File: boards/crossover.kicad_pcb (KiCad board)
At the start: 2 copper layers, 160 x 105.4 mm, 61 parts, among them J1 JACK_TRS_6PINS, P1 12-0-12, U1 TL072, U2 TL074, U3 TDA7292, U4 TL074

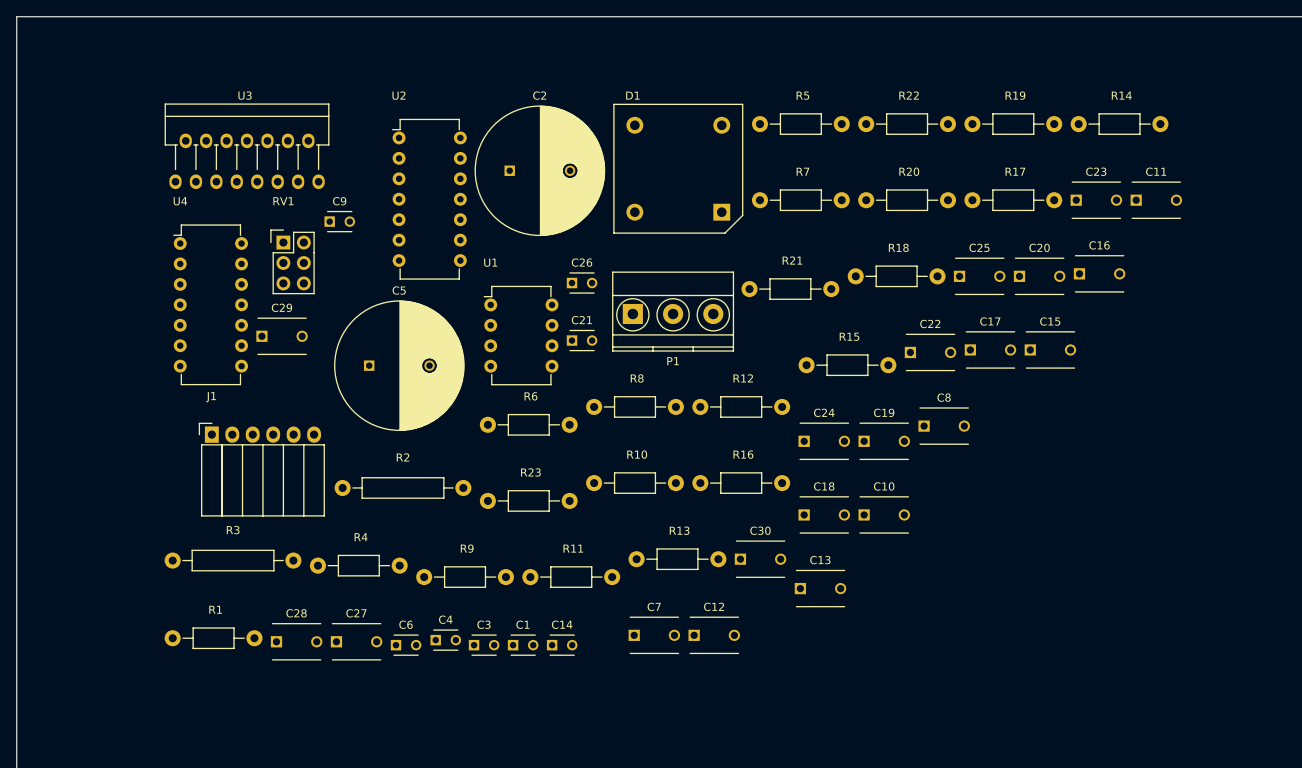
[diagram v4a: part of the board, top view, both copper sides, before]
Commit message: first working impedance measurements
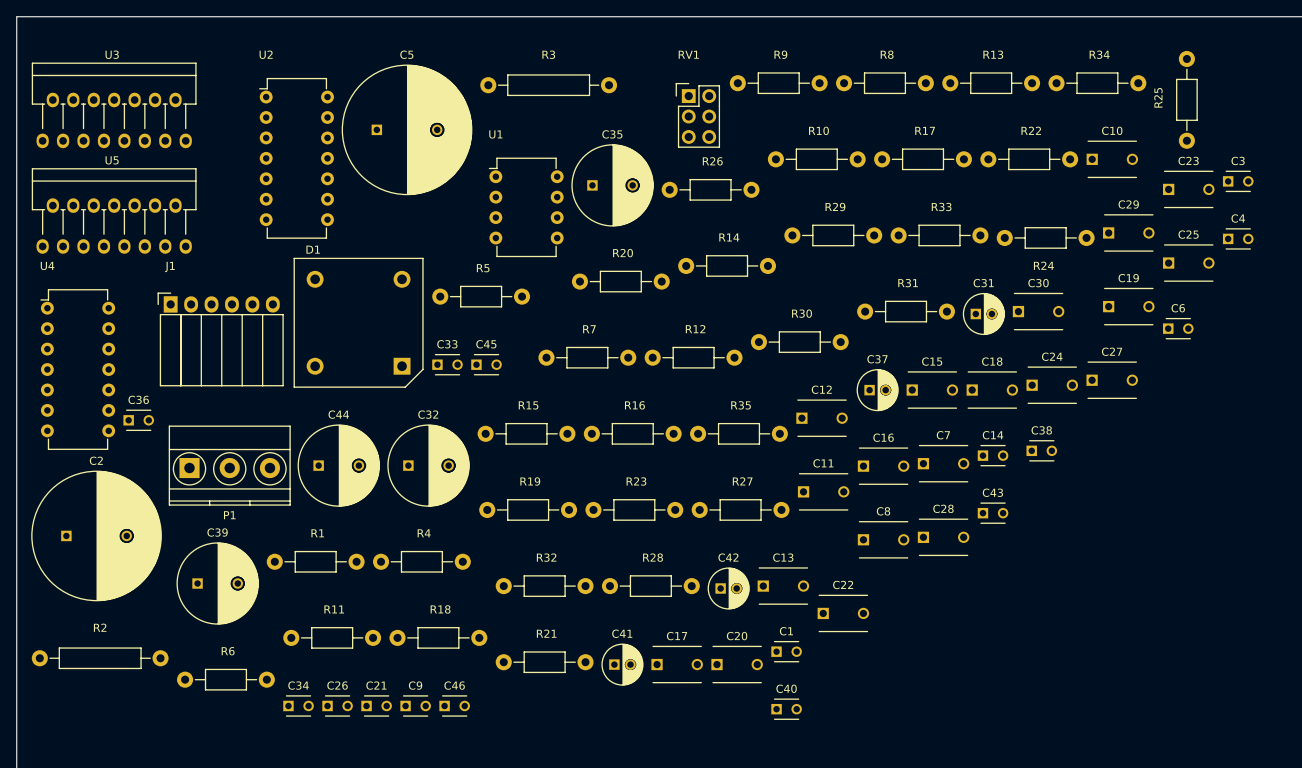
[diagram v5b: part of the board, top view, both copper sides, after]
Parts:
- added C31: CP, Capacitors_ThroughHole:C_Radial_D5_L11_P2, F.Cu at (210.6, 90.3)
- added C32: 1000u, Capacitors_ThroughHole:C_Radial_D10_L20_P5, F.Cu at (140.1, 109.1)
- added C33: 100n, Capacitors_ThroughHole:C_Disc_D3_P2.5, F.Cu at (143.7, 96.6)
- added C34: 100n, Capacitors_ThroughHole:C_Disc_D3_P2.5, F.Cu at (125.2, 139.0)
- added C35: 1000u, Capacitors_ThroughHole:C_Radial_D10_L20_P5, F.Cu at (163.0, 74.3)
- added C36: 100n, Capacitors_ThroughHole:C_Disc_D3_P2.5, F.Cu at (105.4, 103.5)
- added C37: CP, Capacitors_ThroughHole:C_Radial_D5_L11_P2, F.Cu at (197.4, 99.7)
- added C38: 100n, Capacitors_ThroughHole:C_Disc_D3_P2.5, F.Cu at (217.6, 107.3)
- added C39: 1000u, Capacitors_ThroughHole:C_Radial_D10_L20_P5, F.Cu at (113.9, 123.8)
- added C40: 100n, Capacitors_ThroughHole:C_Disc_D3_P2.5, F.Cu at (185.9, 139.4)
- added C41: CP, Capacitors_ThroughHole:C_Radial_D5_L11_P2, F.Cu at (165.7, 133.9)
- added C42: CP, Capacitors_ThroughHole:C_Radial_D5_L11_P2, F.Cu at (178.9, 124.4)
- added C43: 100n, Capacitors_ThroughHole:C_Disc_D3_P2.5, F.Cu at (211.5, 115.0)
- added C44: 1000u, Capacitors_ThroughHole:C_Radial_D10_L20_P5, F.Cu at (129.0, 109.1)
- added C45: 100n, Capacitors_ThroughHole:C_Disc_D3_P2.5, F.Cu at (148.6, 96.6)
- added C46: 100n, Capacitors_ThroughHole:C_Disc_D3_P2.5, F.Cu at (144.6, 139.0)
- added R24: 18K, Resistors_ThroughHole:Resistor_Horizontal_RM10mm, F.Cu at (224.4, 80.8)
- added R25: 560R, Resistors_ThroughHole:Resistor_Horizontal_RM10mm, F.Cu at (236.9, 68.8)
- added R26: 4.8R, Resistors_ThroughHole:Resistor_Horizontal_RM10mm, F.Cu at (172.6, 74.9)
- added R27: 18K, Resistors_ThroughHole:Resistor_Horizontal_RM10mm, F.Cu at (176.3, 114.6)
- added R28: 4.8R, Resistors_ThroughHole:Resistor_Horizontal_RM10mm, F.Cu at (165.2, 124.1)
- added R29: 560R, Resistors_ThroughHole:Resistor_Horizontal_RM10mm, F.Cu at (187.8, 80.5)
- added R30: 18K, Resistors_ThroughHole:Resistor_Horizontal_RM10mm, F.Cu at (183.7, 93.8)
- added R31: 4.8R, Resistors_ThroughHole:Resistor_Horizontal_RM10mm, F.Cu at (196.9, 90.0)
- added R32: 560R, Resistors_ThroughHole:Resistor_Horizontal_RM10mm, F.Cu at (152.0, 124.1)
- added R33: 18K, Resistors_ThroughHole:Resistor_Horizontal_RM10mm, F.Cu at (201.0, 80.5)
- added R34: 4.8R, Resistors_ThroughHole:Resistor_Horizontal_RM10mm, F.Cu at (220.7, 61.6)
- added R35: 560R, Resistors_ThroughHole:Resistor_Horizontal_RM10mm, F.Cu at (176.1, 105.2)
- added U5: TDA7292, TO_SOT_Packages_THT:Multiwatt_15_Vertical, F.Cu at (94.7, 81.9)
- moved C4 110.4 mm to (242.0, 81.0)
- moved C3 110.0 mm to (242.0, 73.8)
- moved C29 106.0 mm to (227.1, 80.2)
- moved C6 103.7 mm to (234.5, 92.1)
- moved C27 99.4 mm to (225.1, 98.5)
- moved C28 81.4 mm to (204.1, 118.0)
- moved R19 77.0 mm to (149.9, 114.6)
- moved R9 72.7 mm to (181.1, 61.6)
- moved R18 72.5 mm to (138.8, 130.5)
- moved C2 71.4 mm to (97.6, 117.9)
- moved R3 70.9 mm to (150.0, 61.9)
- moved R13 70.8 mm to (207.5, 61.6)
- moved C20 61.2 mm to (178.5, 133.8)
- moved C9 60.9 mm to (139.8, 139.0)
- moved C26 60.7 mm to (130.1, 139.0)
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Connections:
- net left_high_out renamed Net-(C42-Pad2)
- net left_low_out renamed Net-(C22-Pad1)
- C10 pad 1: right_low_out -> Net-(C10-Pad1)
- C11 pad 1: right_low_out -> Net-(C10-Pad1)
- R9 pad 2: right_high_out -> Net-(C37-Pad2)
- U2 pad 13: right_high_out -> Net-(C37-Pad2)
- U2 pad 14: right_high_out -> Net-(C37-Pad2)
- U2 pad 6: right_low_out -> Net-(C10-Pad1)
- U2 pad 7: right_low_out -> Net-(C10-Pad1)
- U3 pad 1: (no net) -> -12V
- U3 pad 10: (no net) -> Net-(R27-Pad1)
- U3 pad 11: (no net) -> Net-(C37-Pad1)
- U3 pad 2: (no net) -> right_high_out
- U3 pad 3: (no net) -> +12V
- U3 pad 4: (no net) -> right_low_out
- U3 pad 6: (no net) -> -12V
- U3 pad 7: (no net) -> Net-(C31-Pad1)
- U3 pad 8: (no net) -> Net-(R24-Pad1)
- U3 pad 9: (no net) -> GND

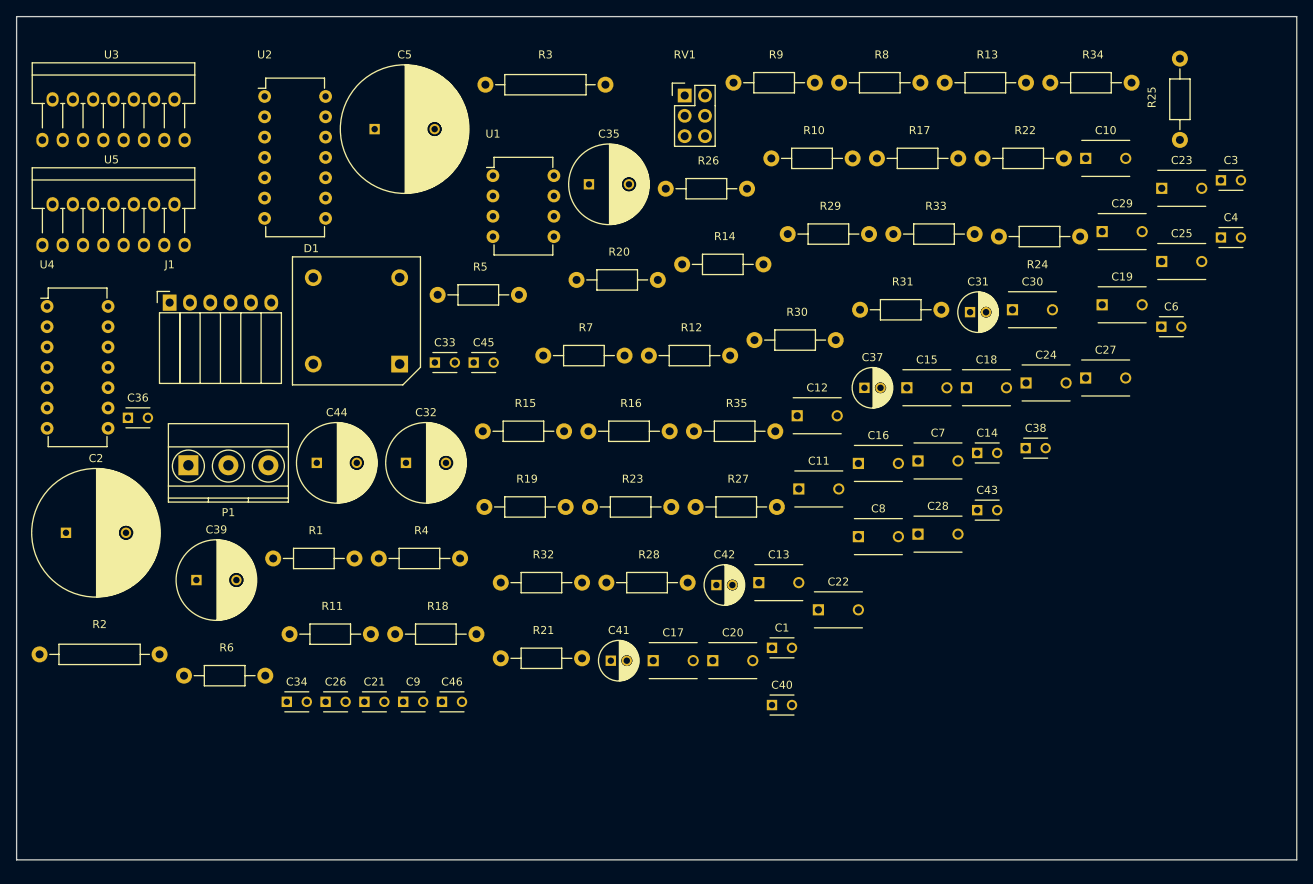
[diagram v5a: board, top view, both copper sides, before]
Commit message: documentation, pcb updates, some pylint fixes
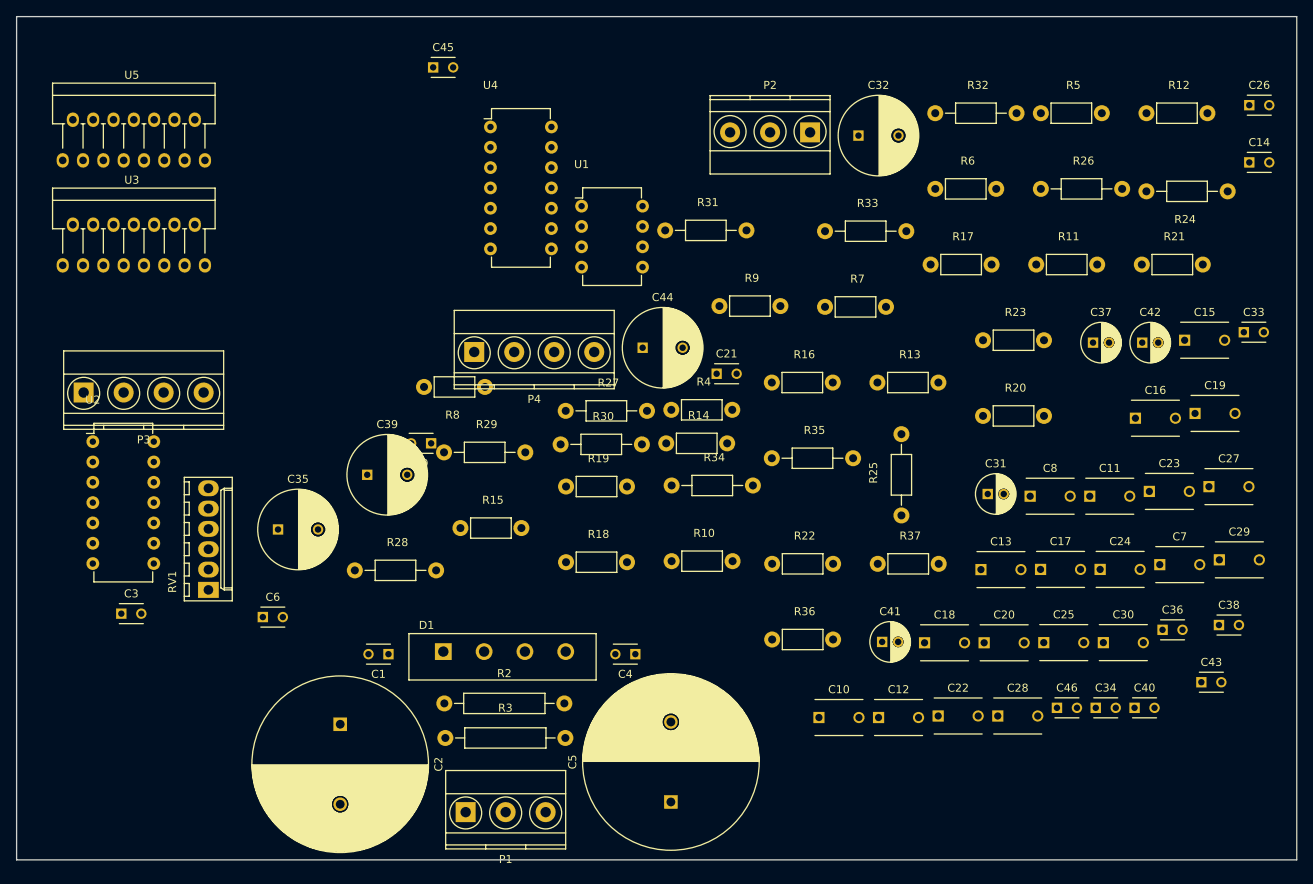
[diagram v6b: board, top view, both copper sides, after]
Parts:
- removed J1: JACK_TRS_6PINS, Socket_Strips:Socket_Strip_Angled_1x06
- removed R1: 100, Resistors_ThroughHole:Resistor_Horizontal_RM10mm
- added P2: CONN_01X03, Terminal_Blocks:TerminalBlock_Pheonix_MKDS1.5-3pol, F.Cu at (190.6, 67.8)
- added P3: CONN_01X04, Terminal_Blocks:TerminalBlock_Pheonix_MKDS1.5-4pol, F.Cu at (99.8, 100.3)
- added P4: CONN_01X04, Terminal_Blocks:TerminalBlock_Pheonix_MKDS1.5-4pol, F.Cu at (148.6, 95.3)
- added R36: 1K, Resistors_ThroughHole:Resistor_Horizontal_RM7mm, F.Cu at (185.9, 131.2)
- added R37: 1K, Resistors_ThroughHole:Resistor_Horizontal_RM7mm, F.Cu at (199.1, 121.7)
- C2, C5: footprint Capacitors_ThroughHole:C_Radial_D16_L31.5_P7.5 -> Capacitors_ThroughHole:C_Radial_D22_L41_P10
- C31, C37, C41, C42: value CP -> 1u
- D1: footprint Diodes_ThroughHole:Diode_Bridge_15.7x15.7 -> Diodes_ThroughHole:Diode_Bridge_18.5x5.5
- P1: value 12-0-12 -> CONN_01X03
- R10, R11, R16, R17, R18, R19, R20, R21, R22, R23, R8, R9: value RH -> R; footprint Resistors_ThroughHole:Resistor_Horizontal_RM10mm -> Resistors_ThroughHole:Resistor_Horizontal_RM7mm
- R12, R13, R14, R15, R4, R5, R6, R7: value RL -> R; footprint Resistors_ThroughHole:Resistor_Horizontal_RM10mm -> Resistors_ThroughHole:Resistor_Horizontal_RM7mm
- RV1: footprint Pin_Headers:Pin_Header_Straight_2x03 -> Connectors_Molex:Molex_KK-6410-06_06x2.54mm_Straight
- moved C3 147.7 mm to (104.5, 128.0)
- moved C26 137.5 mm to (245.5, 64.4)
- moved C36 132.0 mm to (234.7, 130.0)
- moved C6 118.0 mm to (122.2, 128.4)
- moved R6 111.9 mm to (206.3, 74.9)
- moved R11 104.1 mm to (218.9, 84.3)
- moved C33 101.2 mm to (244.8, 92.8)
- moved C34 101.1 mm to (226.3, 139.7)
- moved R21 94.0 mm to (232.1, 84.3)
- moved C5 91.9 mm to (173.2, 151.5), turned to 90 degrees
- moved C4 89.8 mm to (168.8, 133.0), turned to 180 degrees
- moved RV1 85.8 mm to (115.4, 125.0), turned to 90 degrees
- moved R3 81.8 mm to (145.0, 143.5)
- moved R32 80.0 mm to (206.3, 65.4)
- moved R5 78.7 mm to (219.5, 65.4)
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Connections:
- net Net-(D1-Pad2) renamed /-12VAC
- net Net-(D1-Pad4) renamed /+12VAC
- net left_high_out renamed /left_high_out
- net left_low_out renamed /left_low_out
- net right_high_out renamed /right_high_out
- net right_low_out renamed /right_low_out
- C32 pad 2: GND -> Net-(C32-Pad2)
- C39 pad 2: GND -> Net-(C39-Pad2)
- RV1 pad 1: Net-(J1-Pad2) -> right_in
- RV1 pad 4: Net-(J1-Pad3) -> left_in
- U3 pad 5: (no net) -> Net-(C32-Pad2)
- U5 pad 5: (no net) -> Net-(C39-Pad2)

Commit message: some board updates
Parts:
- added C47: 1000u, Capacitors_ThroughHole:C_Radial_D10_L20_P5, F.Cu at (287.0, 84.8)
- added C48: 100n, Capacitors_ThroughHole:C_Disc_D3_P2.5, F.Cu at (149.1, 72.5)
- added C49: 100n, Capacitors_ThroughHole:C_Disc_D6_P5, F.Cu at (143.4, 68.3)
- added C50: 100n, Capacitors_ThroughHole:C_Disc_D3_P2.5, F.Cu at (162.9, 74.0)
- added C51: 100n, Capacitors_ThroughHole:C_Disc_D6_P5, F.Cu at (142.9, 79.6)
- added C52: 100n, Capacitors_ThroughHole:C_Disc_D6_P5, F.Cu at (168.0, 66.7)
- added C53: 100n, Capacitors_ThroughHole:C_Disc_D6_P5, F.Cu at (168.4, 78.4)
- added C54: 100n, Capacitors_ThroughHole:C_Disc_D3_P2.5, F.Cu at (107.4, 88.9)
- added C55: 100n, Capacitors_ThroughHole:C_Disc_D3_P2.5, F.Cu at (109.0, 73.4)
- added R1: 2K2, Resistors_ThroughHole:Resistor_Horizontal_RM7mm, F.Cu at (138.4, 75.9)
- added R38: Rph, Resistors_ThroughHole:Resistor_Horizontal_RM7mm, F.Cu at (140.8, 60.7)
- added R39: 2K2, Resistors_ThroughHole:Resistor_Horizontal_RM7mm, F.Cu at (149.5, 84.5)
- added R40: 2K2, Resistors_ThroughHole:Resistor_Horizontal_RM7mm, F.Cu at (157.2, 88.0)
- added R41: Rph, Resistors_ThroughHole:Resistor_Horizontal_RM7mm, F.Cu at (138.3, 87.2)
- added R42: 2K2, Resistors_ThroughHole:Resistor_Horizontal_RM7mm, F.Cu at (172.0, 59.6)
- added R43: 2K2, Resistors_ThroughHole:Resistor_Horizontal_RM7mm, F.Cu at (160.4, 61.0)
- added R44: 2K2, Resistors_ThroughHole:Resistor_Horizontal_RM7mm, F.Cu at (172.0, 77.9)
- added R45: 2K2, Resistors_ThroughHole:Resistor_Horizontal_RM7mm, F.Cu at (172.1, 88.6)
- added R46: Rph, Resistors_ThroughHole:Resistor_Horizontal_RM7mm, F.Cu at (150.9, 58.2)
- added R47: Rph, Resistors_ThroughHole:Resistor_Horizontal_RM7mm, F.Cu at (168.4, 87.9)
- added R48: Rbs1, Resistors_ThroughHole:Resistor_Horizontal_RM7mm, F.Cu at (107.3, 92.8)
- added R49: Rbs2, Resistors_ThroughHole:Resistor_Horizontal_RM7mm, F.Cu at (110.1, 92.8)
- added R50: Rbs1, Resistors_ThroughHole:Resistor_Horizontal_RM7mm, F.Cu at (120.7, 70.1)
- added R51: Rbs2, Resistors_ThroughHole:Resistor_Horizontal_RM7mm, F.Cu at (113.0, 67.1)
- added RV2: 1K POT, Potentiometers:Potentiometer_Bourns_3339P_Angular_ScrewUp, F.Cu at (253.1, 111.1)
- added RV3: 1K POT, Potentiometers:Potentiometer_Bourns_3339P_Angular_ScrewUp, F.Cu at (264.5, 101.5)
- added U6: TL074, Housings_DIP:DIP-14_W7.62mm, F.Cu at (152.4, 65.8)
- R24, R30: value 18K -> 68K
- R25, R32: value 560R -> 1K5
- R37: value 1K -> 2K2
- moved C9 219.8 mm to (363.0, 103.8)
- moved C45 203.5 mm to (337.0, 122.7)
- moved C12 200.7 mm to (381.8, 57.8)
- moved R22 196.3 mm to (371.4, 57.8)
- moved R15 193.5 mm to (336.2, 76.7)
- moved R4 192.8 mm to (360.8, 57.8)
- moved C21 192.1 mm to (371.0, 93.7)
- moved C39 185.7 mm to (314.1, 60.6)
- moved R8 185.1 mm to (334.9, 91.8)
- moved R30 184.1 mm to (336.9, 57.8)
- moved R28 183.0 mm to (309.8, 72.5)
- moved R27 179.6 mm to (336.2, 67.3)
- moved R16 177.0 mm to (360.0, 67.3)
- moved R36 169.9 mm to (346.8, 76.7)
- moved C28 169.4 mm to (370.8, 76.4)
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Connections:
- C15 pad 2: right_in -> /right_tweeter_ph
- C27 pad 2: left_in -> /left_tweeter_ph
- C32 pad 2: Net-(C32-Pad2) -> /1s_delay
- C39 pad 2: Net-(C39-Pad2) -> GND
- P2 pad 1: left_in -> /left_in
- P2 pad 3: right_in -> /right_in
- R12 pad 1: left_in -> /left_woofer_in
- R25 pad 2: Net-(R24-Pad1) -> Net-(R25-Pad2)
- R32 pad 2: Net-(R30-Pad1) -> Net-(R32-Pad2)
- R36 pad 1: Net-(C32-Pad2) -> /1s_delay
- R37 pad 1: GND -> Net-(C51-Pad1)
- R37 pad 2: Net-(C39-Pad2) -> Net-(R1-Pad1)
- R4 pad 1: right_in -> /right_woofer_in
- RV1 pad 1: right_in -> /right_in
- RV1 pad 4: left_in -> /left_in
- U1 pad 1: left_in -> /right_woofer_in
- U1 pad 2: left_in -> Net-(C54-Pad2)
- U1 pad 6: right_in -> Net-(C55-Pad2)
- U1 pad 7: right_in -> /left_woofer_in
- U3 pad 5: Net-(C32-Pad2) -> /1s_delay
- U3 pad 8: Net-(R24-Pad1) -> Net-(RV2-Pad2)
- U5 pad 5: Net-(C39-Pad2) -> /1s_delay
- U5 pad 8: Net-(R30-Pad1) -> Net-(RV3-Pad2)
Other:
- board text added: "input section"
- board text added: "power section"

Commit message: updated board
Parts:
- C54, C55: footprint Capacitors_ThroughHole:C_Disc_D3_P2.5 -> Capacitors_ThroughHole:C_Disc_D6_P5
- U3, U5: footprint TO_SOT_Packages_THT:Multiwatt_15_Vertical -> TO_SOT_Packages_THT:Multiwatt-11_Vertical_StaggeredType1
- moved C12 305.1 mm to (78.4, 25.4), turned to 90 degrees
- moved C17 301.3 mm to (70.1, 43.0)
- moved C13 298.1 mm to (69.5, 28.5), turned to 90 degrees
- moved C26 294.2 mm to (89.6, 63.4), turned to 180 degrees
- moved C15 294.1 mm to (61.8, 43.9), turned to 270 degrees
- moved C9 293.3 mm to (79.6, 28.1)
- moved C7 291.5 mm to (90.0, 21.2)
- moved C16 289.9 mm to (74.8, 48.2), turned to 180 degrees
- moved C14 288.4 mm to (83.9, 42.0)
- moved C8 286.9 mm to (89.9, 26.8)
- moved C21 284.2 mm to (87.2, 77.6)
- moved C11 279.9 mm to (65.4, 21.4), turned to 180 degrees
- moved C28 278.7 mm to (92.4, 62.0)
- moved C23 275.9 mm to (102.3, 78.1)
- moved C18 274.6 mm to (85.2, 44.9), turned to 270 degrees
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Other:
- board size 160 x 105.4 mm -> 185.4 x 105.4 mm
- net class Audio Out: trace_width 1.27 -> 0.635
- net class Power: trace_width 2.54 -> 1.27
